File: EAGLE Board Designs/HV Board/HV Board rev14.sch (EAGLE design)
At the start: 104 parts, among them J1 JUMPER.1, Q1 TRANSISTOR_N_MOS_2-7K1S_TK6P6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, U1 HM2102NLT, U10 CDSOT23-T24CAN-Q, U11 TXB0104TSSOP, U12 CAN_TRANSCIEVER_TCAN1051HQV-Q1, U13 CPC1002N, U14 CPC1002N, U15 VOLTAGE_REGULATOR_SOT89_12V, U16 CPC1002N, U17 CPC1002N, U18 VOLTAGE_REGULATOR_SOT89_12V, U2 OPAMP_1_CHANNEL_OPA991, U3 OPAMP_1_CHANNEL_OPA991, U4 OPAMP_1_CHANNEL_OPA991, U5 OKI-78SR-5, U6 LTC6820, U7 MCP3204, U8 STWD100PYW83F, U9 SN74LVC1G08

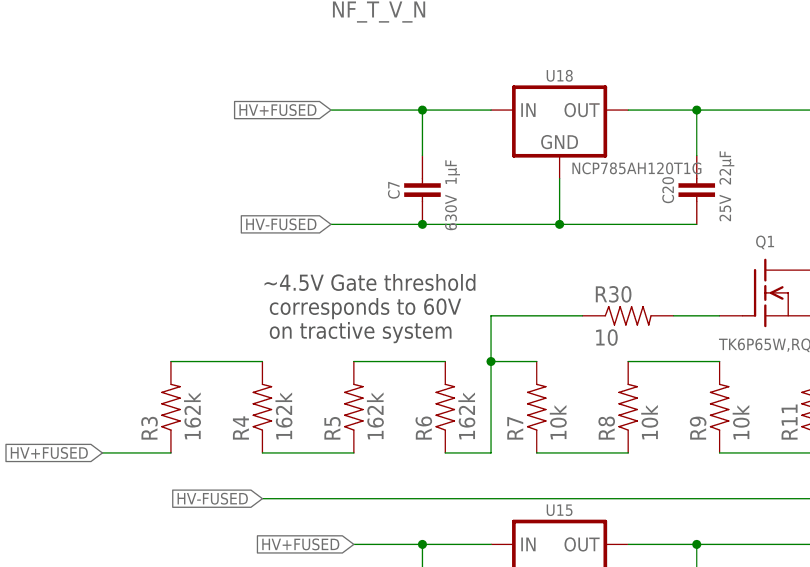
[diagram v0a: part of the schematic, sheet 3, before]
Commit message: New bspd resistor values (#1)
* New bspd resistor values

* Fixed HV board rev14 schematic note
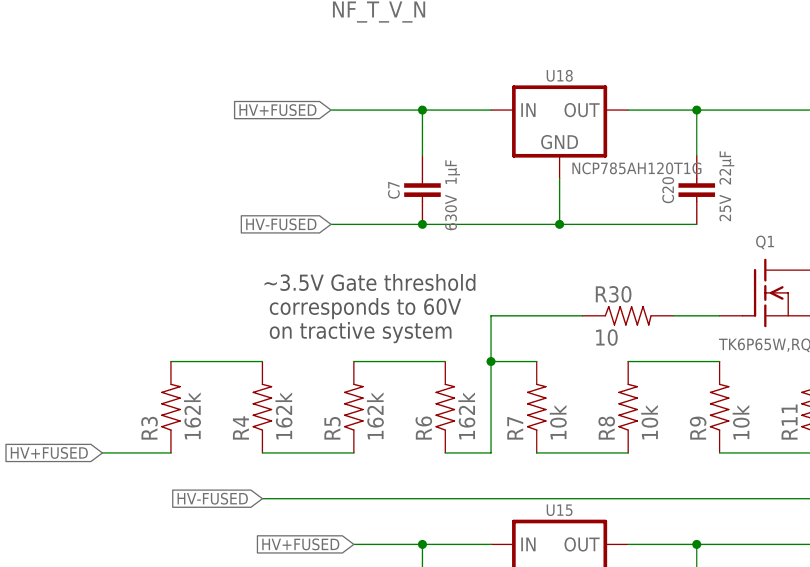
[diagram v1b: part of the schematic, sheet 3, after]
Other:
- note added: "~3.5V Gate threshold corresponds to 60V on tractive system"
- note removed: "~4.5V Gate threshold corresponds to 60V on tractive system"
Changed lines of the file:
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@@
 <text x="134.62" y="137.16" size="1.778" layer="97">Capacitor used
 for Precharge</text>
-<text x="33.02" y="71.12" size="1.778" layer="97">~4.5V Gate threshold
+<text x="33.02" y="71.12" size="1.778" layer="97">~3.5V Gate threshold
  corresponds to 60V
  on tractive system</text>
